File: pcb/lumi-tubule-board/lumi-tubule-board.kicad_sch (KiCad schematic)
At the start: 74 parts, among them Q1 DMN1045UFR4, Q10 DMN1045UFR4, Q11 DMN1045UFR4, Q12 DMN1045UFR4, Q13 DMN1045UFR4, Q2 DMN1045UFR4, Q3 DMN1045UFR4, Q4 DMN1045UFR4, Q5 DMN1045UFR4, Q6 DMN1045UFR4, Q7 DMN1045UFR4, Q8 DMN1045UFR4, Q9 DMN1045UFR4, SW1 SWITCH_TACT_SMT4.6X2.8, SW2 SWITCH_TACT_SMT4.6X2.8, U1 SHTC3, U2 VREG_SOT23-5, U3 ESP32-S3-MINI-1, U4 LIS2Dx12, X1 USB_C

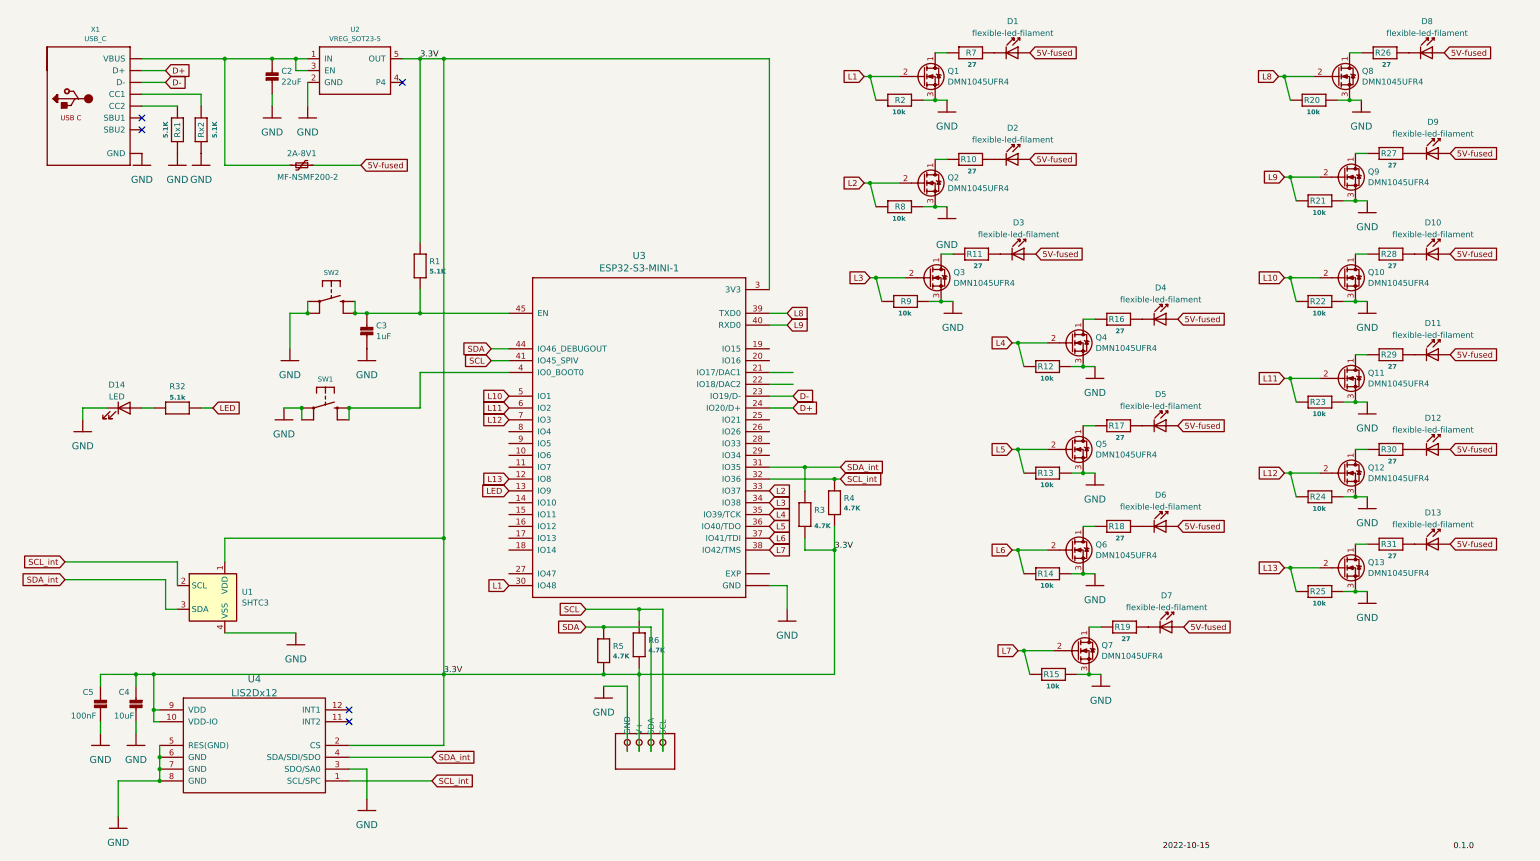
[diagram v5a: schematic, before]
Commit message: Rough layout with TLC59108
Made  rough layout with the TLC59108 LED drivers (2 on the board). Routing is now a lot easier. Still some minor issues to be ironed out. Schematic is complete; PCB layout still needs routing work.
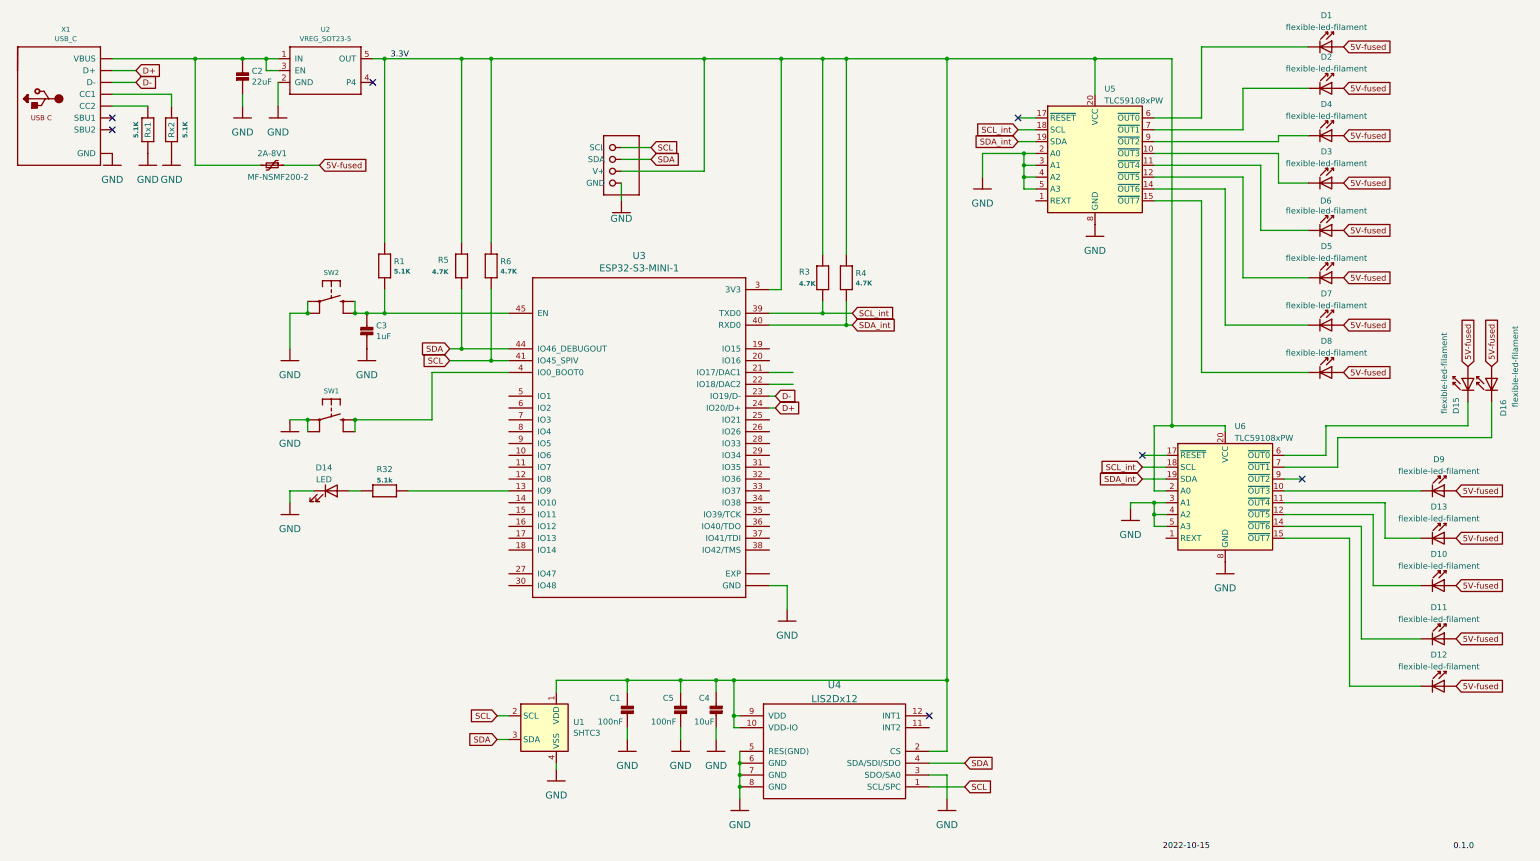
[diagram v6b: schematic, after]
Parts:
- removed Q1, Q10, Q11, Q12, Q13, Q2, Q3, Q4, Q5, Q6, Q7, Q8, Q9: DMN1045UFR4, lumi-tubule-board:DMN1045UFR4, symbol other-parts:DMN1045UFR4
- removed R10, R11, R16, R17, R18, R19, R26, R27, R28, R29, R30, R31, R7: 27, Resistor_SMD:R_0805_2012Metric, symbol Adafruit_ESP32-S3_8MB_No_PSRAM-eagle-import:RESISTOR_0603_NOOUT
- removed R12, R13, R14, R15, R2, R20, R21, R22, R23, R24, R25, R8, R9: 10k, Resistor_SMD:R_0402_1005Metric, symbol Adafruit_ESP32-S3_8MB_No_PSRAM-eagle-import:RESISTOR_0603_NOOUT
- added C1: 100nF, Capacitor_SMD:C_0402_1005Metric, symbol Adafruit_ESP32-S3_8MB_No_PSRAM-eagle-import:CAP_CERAMIC_0402
- added D15, D16: flexible-led-filament, lumi-tubule-board:Flexible LED filament viamount, symbol lumi-tubule-board:flexible-led-filament
- added U5, U6: TLC59108xPW, Package_SO:TSSOP-20_4.4x6.5mm_P0.65mm, symbol Driver_LED:TLC59108xPW
- renumbered D11 to D10, D12 to D11, D13 to D12, D10 to D13, D4 to D3, D3 to D4, D6 to D5, D5 to D6
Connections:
- net L8 is gone; now on net SCL_int: U3.39 (TXD0)
- net L9 is gone; now on net SDA_int: U3.40 (RXD0)
- net 3.3V: now also R3.1, R4.1, R5.1, R6.1, C1.2, U5.20 (VCC), U6.2 (A0), U6.20 (VCC); no longer R3.2, R4.2, R5.2, R6.2
- net 5V-fused: now also D15.2 (A), D16.2 (A)
- net GND: now also C1.1, U5.13 (GND), U5.16 (GND), U5.2 (A0), U5.3 (A1), U5.4 (A2), U5.5 (A3), U5.8 (GND), U6.13 (GND), U6.16 (GND), U6.3 (A1), U6.4 (A2), U6.5 (A3), U6.8 (GND)
- net SCL: now also R6.2, U1.2 (SCL), U4.1 (SCL/SPC); no longer R6.1
- net SCL_int: now also R3.2, U5.18 (SCL), U6.18 (SCL); no longer R4.1, U1.2 (SCL), U3.32 (IO36), U4.1 (SCL/SPC)
- net SDA: now also R5.2, U1.3 (SDA), U4.4 (SDA/SDI/SDO); no longer R5.1
- net SDA_int: now also R4.2, U5.19 (SDA), U6.19 (SDA); no longer R3.1, U1.3 (SDA), U3.31 (IO35), U4.4 (SDA/SDI/SDO)
- net at D1.1 (K): now also U5.6 (~{OUT0})
- net at D13.1 (K): now also U6.11 (~{OUT4})
- net at D10.1 (K): now also U6.12 (~{OUT5})
- net at D2.1 (K): now also U5.7 (~{OUT1})
- net at D4.1 (K): now also U5.9 (~{OUT2})
- net at D11.1 (K): now also U6.14 (~{OUT6})
- net at D8.1 (K): now also U5.15 (~{OUT7})
- net at D3.1 (K): now also U5.10 (~{OUT3})
- net at D7.1 (K): now also U5.14 (~{OUT6})
- net at D12.1 (K): now also U6.15 (~{OUT7})
- net at D9.1 (K): now also U6.10 (~{OUT3})
- net at D5.1 (K): now also U5.12 (~{OUT5})
- net at D6.1 (K): now also U5.11 (~{OUT4})
- net L1: no longer names the net of U3.30 (IO48)
- net L10: no longer names the net of U3.5 (IO1)
- net L11: no longer names the net of U3.6 (IO2)
- net L12: no longer names the net of U3.7 (IO3)
- net L13: no longer names the net of U3.12 (IO8)
- net L2: no longer names the net of U3.33 (IO37)
- net L3: no longer names the net of U3.34 (IO38)
- net L4: no longer names the net of U3.35 (IO39/TCK)
- net L5: no longer names the net of U3.36 (IO40/TDO)
- net L6: no longer names the net of U3.37 (IO41/TDI)
- net L7: no longer names the net of U3.38 (IO42/TMS)
- net LED: no longer names the net of R32.2, U3.13 (IO9)
- new net: D16.1 (K), U6.7 (~{OUT1})
- new net: D15.1 (K), U6.6 (~{OUT0})
- no-connect marks 5 -> 7
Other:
- moved on the sheet: 2A-8V1, C2, C4, C5, D1, D10, D11, D12, D13, D14, D2, D3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

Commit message: Complete TLC59018 implementaiton
Fully routed board which should theoretically need only cosmetic alterations. Some issues with soldermask goign outside the board (might cause manufacturer to get upset).
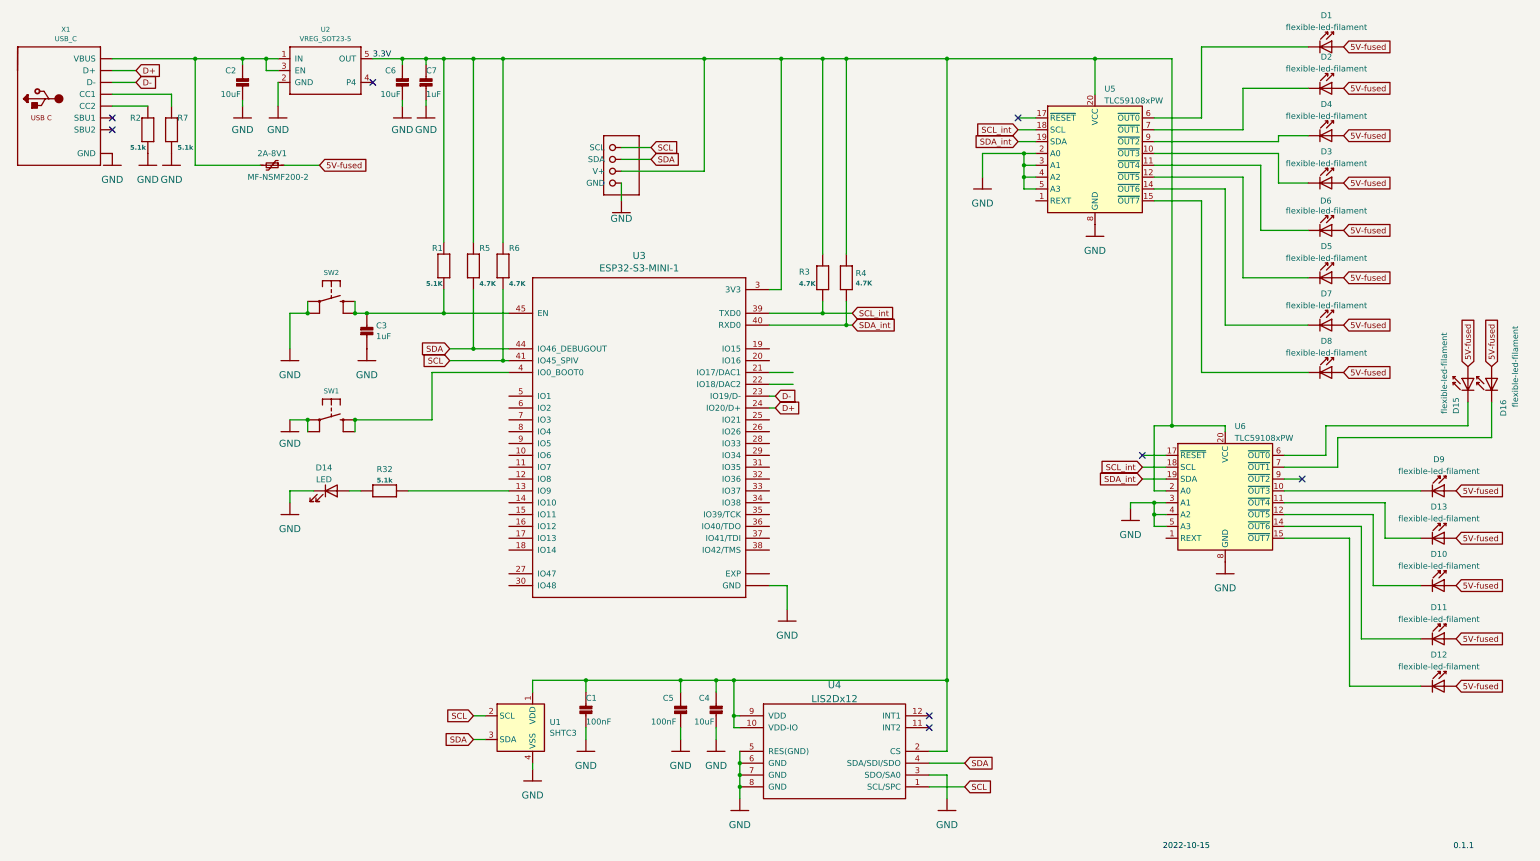
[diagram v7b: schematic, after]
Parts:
- removed C2: 22uF, Capacitor_SMD:C_0603_1608Metric, symbol Adafruit_ESP32-S3_8MB_No_PSRAM-eagle-import:CAP_CERAMIC_0402NO
- removed Rx1, Rx2: 5.1K, Resistor_SMD:R_0805_2012Metric, symbol Adafruit_ESP32-S3_8MB_No_PSRAM-eagle-import:RESISTOR_0603_NOOUT
- added C2, C6: 10uF, Capacitor_SMD:C_0805_2012Metric, symbol Adafruit_ESP32-S3_8MB_No_PSRAM-eagle-import:CAP_CERAMIC_0402
- added C7: 1uF, Capacitor_SMD:C_0603_1608Metric, symbol Adafruit_ESP32-S3_8MB_No_PSRAM-eagle-import:CAP_CERAMIC_0402NO
- added R2, R7: 5.1k, Resistor_SMD:R_0603_1608Metric, symbol Adafruit_ESP32-S3_8MB_No_PSRAM-eagle-import:RESISTOR_0603
- C3: footprint Capacitor_SMD:C_1206_3216Metric -> Capacitor_SMD:C_0603_1608Metric; JLCPCB ref C1848 -> C15849
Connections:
- net 3.3V: now also C6.2, C7.1
- net GND: now also C2.1, C6.1, C7.2, R2.2, R7.2
- net at 2A-8V1.2, U2.1 (IN), U2.3 (EN)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: now also C2.2
- net at X1.A5 (CC1): now also R7.1
- net at X1.B5 (CC2): now also R2.1
- no-connect marks 7 -> 8
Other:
- moved on the sheet: C1, R1, R5, R6, U1

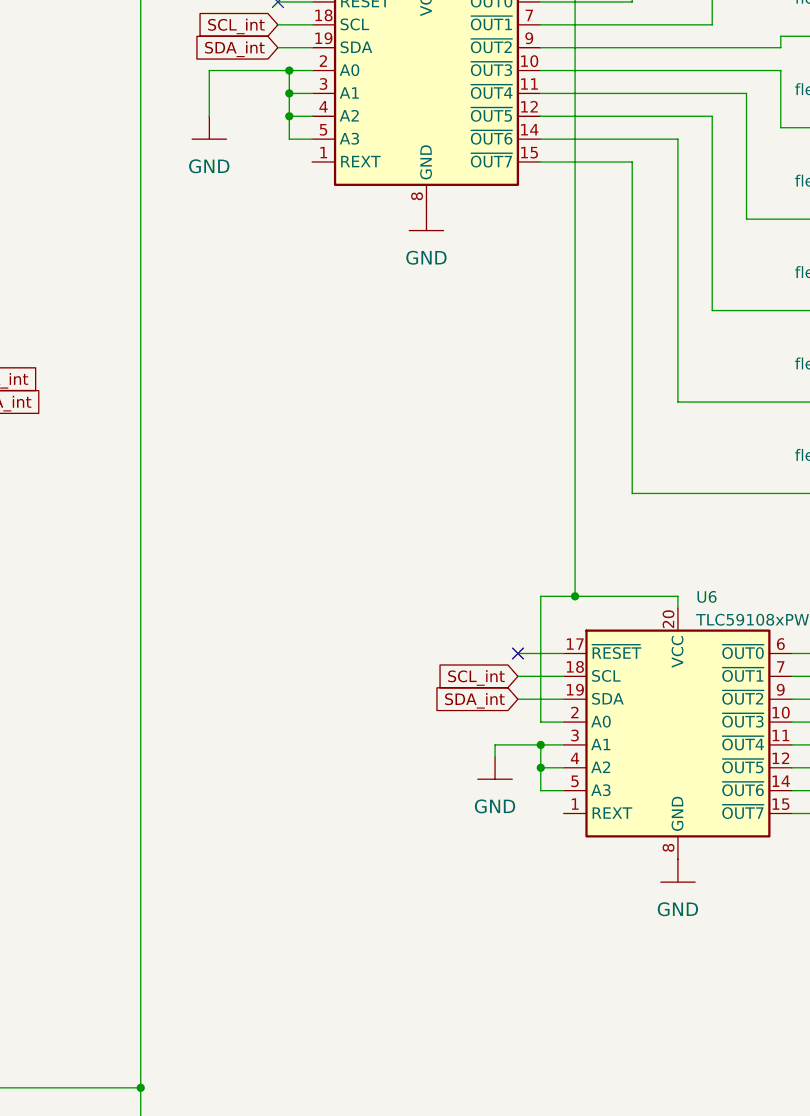
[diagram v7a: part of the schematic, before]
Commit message: Add current settings resistors to TLC59108
Add 187ohm resistors to set current tartget on TLC59108
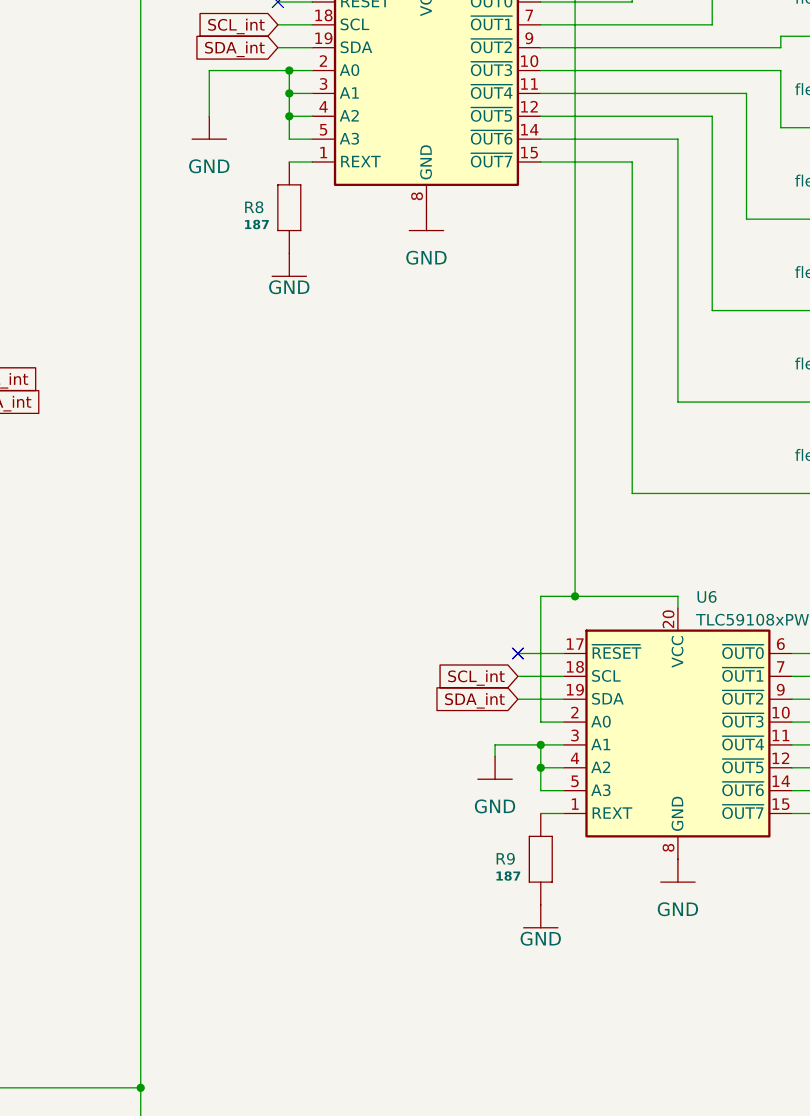
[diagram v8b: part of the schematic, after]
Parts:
- added R8, R9: 187, Resistor_SMD:R_0402_1005Metric, symbol Adafruit_ESP32-S3_8MB_No_PSRAM-eagle-import:RESISTOR_0402
- U5, U6: JLCPCB ref (none) -> C130031
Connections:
- net GND: now also R8.2, R9.2
- net at U5.1 (REXT): now also R8.1
- net at U6.1 (REXT): now also R9.1
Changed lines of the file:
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@@
+    (stroke (width 0) (type default) (color 0 0 0 0))
+  )
+  (wire (pts (xy 257.81 127) (xy 260.35 127))
     (stroke (width 0) (type default) (color 0 0 0 0))
   )
@@
   )
   (wire (pts (xy 257.81 54.61) (xy 267.97 54.61))
+    (stroke (width 0) (type default) (color 0 0 0 0))
+  )
+  (wire (pts (xy 229.87 54.61) (xy 232.41 54.61))
     (stroke (width 0) (type default) (color 0 0 0 0))
   )
@@
     (pin "2")
   )
+  (symbol (lib_id "Adafruit_ESP32-S3_8MB_No_PSRAM-eagle-import:RESISTOR_0402") (at 229.87 59.69 270) (unit 1)
+    (in_bom yes) (on_board yes)
+    (property "Reference" "R8" (id 0) (at 224.79 59.69 90)
+      (effects (font (size 1.27 1.27)) (justify left))
+    )
+    (property "Value" "187" (id 1) (at 224.79 61.595 90)
+      (effects (font (size 1.016 1.016) bold) (justify left))
+    )
+    (property "Footprint" "Resistor_SMD:R_0402_1005Metric" (id 2) (at 229.87 59.69 0)
+      (effects (font (size 1.27 1.27)) hide)
+    )
+    (property "Datasheet" "https://datasheet.lcsc.com/lcsc/1810231218_YAGEO-AC0402FR-07178RL_C226817.pdf" (id 3) (at 229.87 59.69 0)
+      (effects (font (size 1.27 1.27)) hide)
+    )
+    (property "JLCPCB ref" "C226817" (id 4) (at 229.87 59.69 90)
+      (effects (font (size 1.27 1.27)) hide)
+    )
+    (pin "1")
+    (pin "2")
+  )
+  (symbol (lib_id "Adafruit_ESP32-S3_8MB_No_PSRAM-eagle-import:RESISTOR_0402") (at 257.81 132.08 270) (unit 1)
+    (in_bom yes) (on_board yes)
+    (property "Reference" "R9" (id 0) (at 252.73 132.08 90)
+      (effects (font (size 1.27 1.27)) (justify left))
+    )
+    (property "Value" "187" (id 1) (at 252.73 133.985 90)
+      (effects (font (size 1.016 1.016) bold) (justify left))
+    )
+    (property "Footprint" "Resistor_SMD:R_0402_1005Metric" (id 2) (at 257.81 132.08 0)
+      (effects (font (size 1.27 1.27)) hide)
+    )
+    (property "Datasheet" "https://datasheet.lcsc.com/lcsc/1810231218_YAGEO-AC0402FR-07178RL_C226817.pdf" (id 3) (at 257.81 132.08 0)
+      (effects (font (size 1.27 1.27)) hide)
+    )
+    (property "JLCPCB ref" "C226817" (id 4) (at 257.81 132.08 90)
+      (effects (font (size 1.27 1.27)) hide)
+    )
+    (pin "1")
+    (pin "2")
+  )
   (symbol (lib_id "lumi-tubule-board:flexible-led-filament") (at 295.91 30.48 0) (unit 1)
     (in_bom yes) (on_board yes) (fields_autoplaced)
@@
     )
     (property "Datasheet" "https://www.ti.com/lit/ds/symlink/tlc59108.pdf" (id 3) (at 240.03 48.26 0)
+      (effects (font (size 1.27 1.27)) hide)
+    )
+    (property "JLCPCB ref" "C130031" (id 4) (at 245.11 46.99 0)
       (effects (font (size 1.27 1.27)) hide)
     )
@@
     (pin "2")
   )
+  (symbol (lib_id "Adafruit_ESP32-S3_8MB_No_PSRAM-eagle-import:GND") (at 229.87 67.31 0) (unit 1)
+    (in_bom yes) (on_board yes)
+    (property "Reference" "#GND07" (id 0) (at 229.87 67.31 0)
+      (effects (font (size 1.27 1.27)) hide)
+    )
+    (property "Value" "GND" (id 1) (at 229.87 68.58 0)
+      (effects (font (size 1.4986 1.4986)))
+    )
+    (property "Footprint" "" (id 2) (at 229.87 67.31 0)
+      (effects (font (size 1.27 1.27)) hide)
+    )
+    (property "Datasheet" "" (id 3) (at 229.87 67.31 0)
+      (effects (font (size 1.27 1.27)) hide)
+    )
+    (pin "1")
+  )
   (symbol (lib_id "Adafruit_ESP32-S3_8MB_No_PSRAM-eagle-import:CAP_CERAMIC_0402") (at 163.83 162.56 180) (unit 1)
     (in_bom yes) (on_board yes)
@@
     )
     (property "Datasheet" "https://www.ti.com/lit/ds/symlink/tlc59108.pdf" (id 3) (at 267.97 120.65 0)
+      (effects (font (size 1.27 1.27)) hide)
+    )
+    (property "JLCPCB ref" "C130031" (id 4) (at 273.05 119.38 0)
       (effects (font (size 1.27 1.27)) hide)
     )
@@
     (pin "2")
   )
+  (symbol (lib_id "Adafruit_ESP32-S3_8MB_No_PSRAM-eagle-import:GND") (at 257.81 139.7 0) (unit 1)
+    (in_bom yes) (on_board yes)
+    (property "Reference" "#GND08" (id 0) (at 257.81 139.7 0)
+      (effects (font (size 1.27 1.27)) hide)
+    )
+    (property "Value" "GND" (id 1) (at 257.81 140.97 0)
+      (effects (font (size 1.4986 1.4986)))
+    )
+    (property "Footprint" "" (id 2) (at 257.81 139.7 0)
+      (effects (font (size 1.27 1.27)) hide)
+    )
+    (property "Datasheet" "" (id 3) (at 257.81 139.7 0)
+      (effects (font (size 1.27 1.27)) hide)
+    )
+    (pin "1")
+  )
   (symbol (lib_id "Adafruit_ESP32-S3_8MB_No_PSRAM-eagle-import:RESISTOR_0603") (at 46.99 39.37 270) (unit 1)
     (in_bom yes) (on_board yes)
@@
       (reference "#GND06") (unit 1) (value "GND") (footprint "")
     )
+    (path "/39e50727-eb8c-4b41-a1e2-782d6e983fc8"
+      (reference "#GND07") (unit 1) (value "GND") (footprint "")
+    )
+    (path "/ac87e252-ecbb-419e-857f-31f9211f5450"
+      (reference "#GND08") (unit 1) (value "GND") (footprint "")
+    )
     (path "/503ce97c-80b8-42ab-a40d-e82c4bb84960"
       (reference "#GND029") (unit 1) (value "GND") (footprint "")
@@
       (reference "R7") (unit 1) (value "5.1k") (footprint "Resistor_SMD:R_0603_1608Metric")
     )
+    (path "/17e331db-e056-4901-ade6-d6acc200365f"
+      (reference "R8") (unit 1) (value "187") (footprint "Resistor_SMD:R_0402_1005Metric")
+    )
+    (path "/1ca7eb37-0a22-48ff-a032-94ed332c9363"
+      (reference "R9") (unit 1) (value "187") (footprint "Resistor_SMD:R_0402_1005Metric")
+    )
     (path "/dec5787c-6a1b-4721-bda6-97b2eff8c935"
